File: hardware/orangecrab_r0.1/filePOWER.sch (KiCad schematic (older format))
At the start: 45 parts, among them J5 Conn_01x02_Male, U1 FAN53541, U10 NCP167, U2 FAN53541, U5 BQ24230, U7 FAN53541, U8 TPS51206

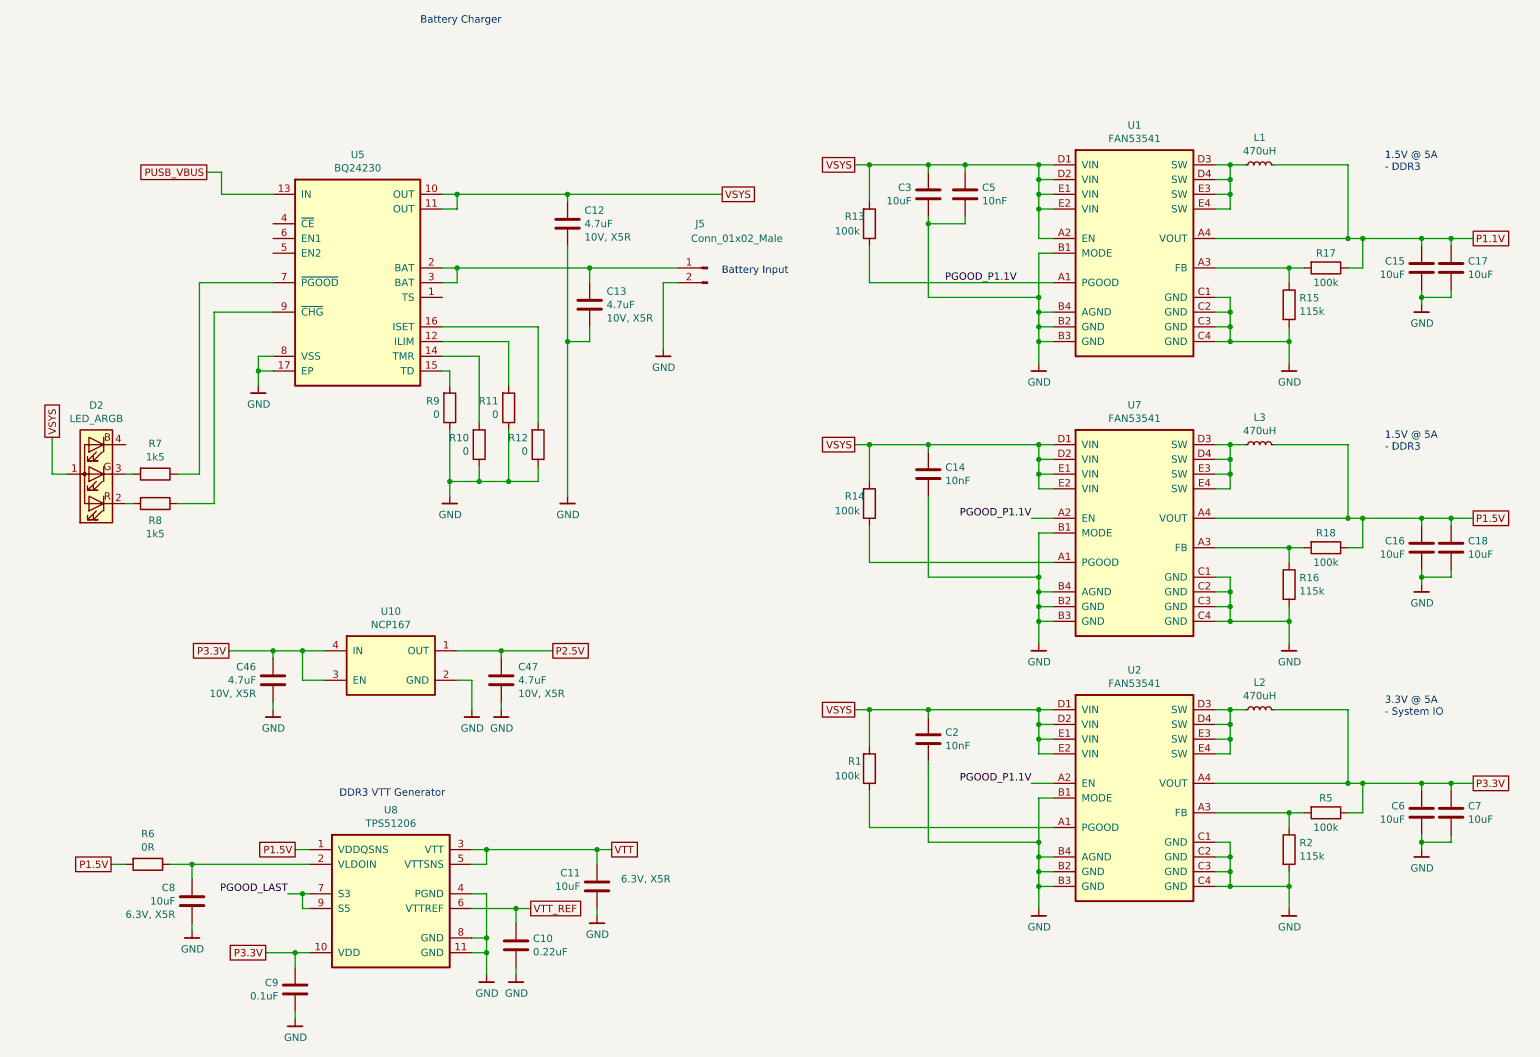
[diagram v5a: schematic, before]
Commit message: Completed 99% of routing.
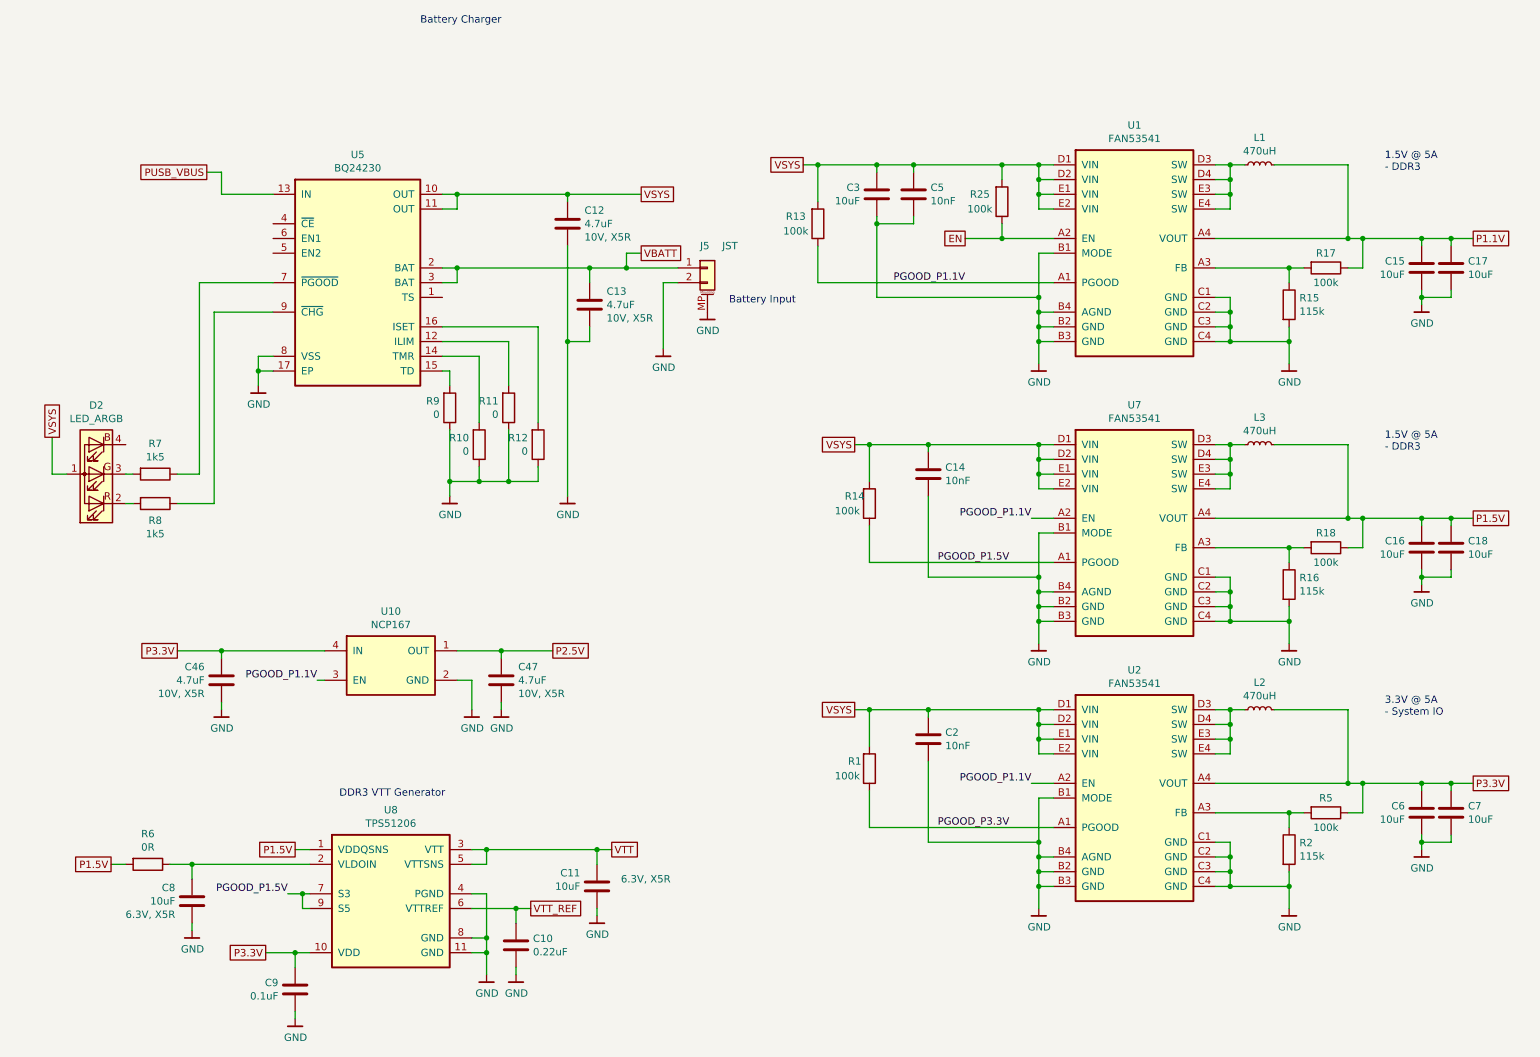
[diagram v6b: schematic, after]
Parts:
- removed J5: Conn_01x02_Male, gkl_conn:JST_PH_B2B-PH-SM4-TB_1x02-1MP_P2.00mm_Vertical, symbol Connector:Conn_01x02_Male
- added J5: JST, gkl_conn:JST_PH_B2B-PH-SM4-TB_1x02-1MP_P2.00mm_Vertical, symbol Connector_Generic_MountingPin:Conn_01x02_MountingPin
- added R25: 100k, Resistor_SMD:R_0201_0603Metric, symbol Device:R
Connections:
- net PGOOD_LAST is gone; now on net PGOOD_P1.5V: U8.7 (S3), U8.9 (S5)
- net GND: now also J5.2 (Pin_2), J5.MP (MountPin)
- net P3.3V: no longer U10.3 (EN)
- net PGOOD_P1.1V: now also U10.3 (EN)
- net VSYS: now also R25.2; no longer U1.A2 (EN)
- net PGOOD_P3.3V: now reaches R1.1, U2.A1 (PGOOD)
- net VBATT: now reaches C13.1, U5.2 (BAT), U5.3 (BAT)
- net VBATT: now also J5.1 (Pin_1)
- net PGOOD_P1.5V: now reaches R14.1, U7.A1 (PGOOD)
- new net EN: R25.1, U1.A2 (EN)
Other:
- moved on the sheet: C3, C46, C5, R13
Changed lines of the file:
@@
 Comment4 ""
 $EndDescr
-Text Notes 6050 1950 2    50   ~ 0
+Text Notes 6100 2150 2    50   ~ 0
 Battery Input
 Text Notes 3550 250  0    50   ~ 0
@@
 $EndComp
 $Comp
-L Connector:Conn_01x02_Male J5
-U 1 1 5D179AC3
-P 5500 1900
-F 0 "J5" H 5550 2200 50  0000 C CNN
-F 1 "Conn_01x02_Male" H 5300 2100 50  0000 C CNN
-F 2 "gkl_conn:JST_PH_B2B-PH-SM4-TB_1x02-1MP_P2.00mm_Vertical" H 5500 1900 50  0001 C CNN
-F 3 "~" H 5500 1900 50  0001 C CNN
-	1    5500 1900
-	-1   0    0    -1
-$EndComp
-$Comp
 L gkl_pmic:FAN53541 U2
 U 1 1 5D171FDD
@@
 $EndComp
 Wire Wire Line
-	7000 5250 7000 5300
-Wire Wire Line
 	7000 5800 7750 5800
 Connection ~ 7750 5800
@@
 Connection ~ 4700 1900
 Wire Wire Line
-	4700 1900 5300 1900
+	4700 1900 4950 1900
 Wire Wire Line
 	4550 1750 4550 2400
@@
 Text GLabel 6500 4900 0    50   UnSpc ~ 0
 VSYS
-Text GLabel 5600 1400 2    50   UnSpc ~ 0
+Text GLabel 5050 1400 2    50   UnSpc ~ 0
 VSYS
 Wire Wire Line
-	5600 1400 4550 1400
+	5050 1400 4550 1400
 Connection ~ 4550 1400
 Wire Wire Line
@@
 	7750 1500 7750 1400
 Wire Wire Line
-	7750 1200 7250 1200
+	7750 1200 7500 1200
 Wire Wire Line
 	7850 1200 7750 1200
@@
 	7750 1400 7750 1300
 Wire Wire Line
-	7850 1700 7750 1700
-Wire Wire Line
 	7850 2400 7750 2400
 Wire Wire Line
@@
 Connection ~ 7750 2200
 Wire Wire Line
-	7850 2000 6600 2000
-Wire Wire Line
-	6600 2000 6600 1750
+	7850 2000 6250 2000
+Wire Wire Line
+	6250 2000 6250 1750
 $Comp
 L Device:R R13
 U 1 1 5D42715D
-P 6600 1600
-F 0 "R13" H 6500 1550 50  0000 C CNN
-F 1 "100k" H 6450 1650 50  0000 C CNN
-F 2 "Resistor_SMD:R_0201_0603Metric" V 6530 1600 50  0001 C CNN
-F 3 "~" H 6600 1600 50  0001 C CNN
-	1    6600 1600
+P 6250 1600
+F 0 "R13" H 6100 1550 50  0000 C CNN
+F 1 "100k" H 6100 1650 50  0000 C CNN
+F 2 "Resistor_SMD:R_0201_0603Metric" V 6180 1600 50  0001 C CNN
+F 3 "~" H 6250 1600 50  0001 C CNN
+	1    6250 1600
 	1    0    0    1
 $EndComp
 Wire Wire Line
-	6600 1450 6600 1200
-Connection ~ 6600 1200
-Wire Wire Line
-	6600 1200 6500 1200
+	6250 1450 6250 1200
+Connection ~ 6250 1200
+Wire Wire Line
+	6250 1200 6150 1200
 $Comp
 L gkl_power:GND #PWR0113
@@
 	1    0    0    -1
 $EndComp
-Text Label 7600 2000 2    50   ~ 0
+Text Label 7250 2000 2    50   ~ 0
 PGOOD_P1.1V
 $Comp
 L Device:C C3
 U 1 1 5D42717F
-P 7000 1400
-F 0 "C3" H 6886 1354 50  0000 R CNN
-F 1 "10uF" H 6886 1445 50  0000 R CNN
-F 2 "Capacitor_SMD:C_0603_1608Metric" H 7038 1250 50  0001 C CNN
-F 3 "~" H 7000 1400 50  0001 C CNN
-	1    7000 1400
+P 6650 1400
+F 0 "C3" H 6536 1354 50  0000 R CNN
+F 1 "10uF" H 6536 1445 50  0000 R CNN
+F 2 "Capacitor_SMD:C_0603_1608Metric" H 6688 1250 50  0001 C CNN
+F 3 "~" H 6650 1400 50  0001 C CNN
+	1    6650 1400
 	1    0    0    1
 $EndComp
@@
 L Device:C C5
 U 1 1 5D427189
-P 7250 1400
-F 0 "C5" H 7135 1354 50  0000 R CNN
-F 1 "10nF" H 7135 1445 50  0000 R CNN
-F 2 "Capacitor_SMD:C_0201_0603Metric" H 7288 1250 50  0001 C CNN
-F 3 "~" H 7250 1400 50  0001 C CNN
-	1    7250 1400
+P 6900 1400
+F 0 "C5" H 6785 1354 50  0000 R CNN
+F 1 "10nF" H 6785 1445 50  0000 R CNN
+F 2 "Capacitor_SMD:C_0201_0603Metric" H 6938 1250 50  0001 C CNN
+F 3 "~" H 6900 1400 50  0001 C CNN
+	1    6900 1400
 	-1   0    0    1
 $EndComp
 Wire Wire Line
-	7250 1550 7250 1600
-Wire Wire Line
-	7250 1600 7000 1600
-Wire Wire Line
-	7000 1600 7000 2100
-Wire Wire Line
-	7000 2100 7750 2100
+	6900 1550 6900 1600
+Wire Wire Line
+	6900 1600 6650 1600
+Wire Wire Line
+	6650 1600 6650 2100
+Wire Wire Line
+	6650 2100 7750 2100
 Connection ~ 7750 2100
 Wire Wire Line
 	7750 2100 7750 2200
 Wire Wire Line
-	7000 1550 7000 1600
-Connection ~ 7000 1600
-Wire Wire Line
-	7000 1250 7000 1200
-Connection ~ 7000 1200
-Wire Wire Line
-	7000 1200 6600 1200
-Wire Wire Line
-	7250 1250 7250 1200
-Connection ~ 7250 1200
-Wire Wire Line
-	7250 1200 7000 1200
+	6650 1550 6650 1600
+Connection ~ 6650 1600
+Wire Wire Line
+	6650 1250 6650 1200
+Connection ~ 6650 1200
+Wire Wire Line
+	6650 1200 6250 1200
+Wire Wire Line
+	6900 1250 6900 1200
+Connection ~ 6900 1200
+Wire Wire Line
+	6900 1200 6650 1200
 Text GLabel 10700 1700 2    50   UnSpc ~ 0
 P1.1V
-Text GLabel 6500 1200 0    50   UnSpc ~ 0
+Text GLabel 6150 1200 0    50   UnSpc ~ 0
 VSYS
 Wire Wire Line
-	7750 1500 7750 1700
-Connection ~ 7750 1500
-Wire Wire Line
 	6600 3100 7000 3100
 Wire Wire Line
 	6600 4900 7000 4900
-Wire Wire Line
-	7000 5300 7000 5800
 $Comp
 L Device:LED_ARGB D2
@@
 Wire Wire Line
 	2800 6250 2750 6250
-Text Label 2650 6150 2    50   ~ 0
-PGOOD_LAST
 Wire Wire Line
 	2800 6150 2750 6150
@@
 L gkl_power:GND #PWR0145
 U 1 1 5D85A10F
-P 2550 4900
-F 0 "#PWR0145" H 2550 4650 50  0001 C CNN
-F 1 "GND" H 2553 4774 50  0000 C CNN
-F 2 "" H 2450 4550 50  0001 C CNN
-F 3 "" H 2550 4900 50  0001 C CNN
-	1    2550 4900
-	1    0    0    -1
-$EndComp
-Wire Wire Line
-	2750 4500 2550 4500
-Connection ~ 2750 4500
-Wire Wire Line
-	2750 4700 2750 4500
-Wire Wire Line
-	2900 4700 2750 4700
+P 2200 4900
+F 0 "#PWR0145" H 2200 4650 50  0001 C CNN
+F 1 "GND" H 2203 4774 50  0000 C CNN
+F 2 "" H 2100 4550 50  0001 C CNN
+F 3 "" H 2200 4900 50  0001 C CNN
+	1    2200 4900
+	1    0    0    -1
+$EndComp
+Wire Wire Line
+	2900 4700 2850 4700
 Wire Wire Line
 	3900 4700 3900 4900
@@
 	4100 4850 4100 4900
 Wire Wire Line
-	2550 4850 2550 4900
-Wire Wire Line
-	2550 4500 2250 4500
-Connection ~ 2550 4500
-Wire Wire Line
-	2550 4550 2550 4500
-Wire Wire Line
-	2900 4500 2750 4500
+	2200 4850 2200 4900
+Wire Wire Line
+	2200 4500 1900 4500
+Connection ~ 2200 4500
+Wire Wire Line
+	2200 4550 2200 4500
 Wire Wire Line
 	4100 4500 4450 4500
@@
 L Device:C C46
 U 1 1 5D757AA5
-P 2550 4700
-F 0 "C46" H 2665 4791 50  0000 L CNN
-F 1 "4.7uF" H 2665 4700 50  0000 L CNN
-F 2 "Capacitor_SMD:C_0402_1005Metric" H 2588 4550 50  0001 C CNN
-F 3 "~" H 2550 4700 50  0001 C CNN
-F 4 "10V, X5R" H 2665 4609 50  0000 L CNN "Info"
-	1    2550 4700
+P 2200 4700
+F 0 "C46" H 2315 4791 50  0000 L CNN
+F 1 "4.7uF" H 2315 4700 50  0000 L CNN
+F 2 "Capacitor_SMD:C_0402_1005Metric" H 2238 4550 50  0001 C CNN
+F 3 "~" H 2200 4700 50  0001 C CNN
+F 4 "10V, X5R" H 2315 4609 50  0000 L CNN "Info"
+	1    2200 4700
 	-1   0    0    -1
 $EndComp
-Text GLabel 2250 4500 0    50   UnSpc ~ 0
+Text GLabel 1900 4500 0    50   UnSpc ~ 0
 P3.3V
 $Comp
@@
 Wire Wire Line
 	7000 3450 7000 4000
+$Comp
+L Connector_Generic_MountingPin:Conn_01x02_MountingPin J5
+U 1 1 5D8317B6
+P 5500 1900
+F 0 "J5" H 5450 2050 50  0000 L CNN
+F 1 "JST" H 5600 2050 50  0000 L CNN
+F 2 "gkl_conn:JST_PH_B2B-PH-SM4-TB_1x02-1MP_P2.00mm_Vertical" H 5500 1900 50  0001 C CNN
+F 3 "~" H 5500 1900 50  0001 C CNN
+	1    5500 1900
+	1    0    0    -1
+$EndComp
+$Comp
+L gkl_power:GND #PWR0166
+U 1 1 5D8325AB
+P 5500 2200
+F 0 "#PWR0166" H 5500 1950 50  0001 C CNN
+F 1 "GND" H 5503 2074 50  0000 C CNN
+F 2 "" H 5400 1850 50  0001 C CNN
+F 3 "" H 5500 2200 50  0001 C CNN
+	1    5500 2200
+	1    0    0    -1
+$EndComp
+Text GLabel 5050 1800 2    50   UnSpc ~ 0
+VBATT
+Wire Wire Line
+	5050 1800 4950 1800
+Wire Wire Line
+	4950 1800 4950 1900
+Wire Wire Line
+	7000 5250 7000 5800
+Connection ~ 4950 1900
+Wire Wire Line
+	4950 1900 5300 1900
+Text Label 2850 4700 2    50   ~ 0
+PGOOD_P1.1V
+Wire Wire Line
+	2200 4500 2900 4500
+Text Label 7550 3900 2    50   ~ 0
+PGOOD_P1.5V
+Text Label 7550 5700 2    50   ~ 0
+PGOOD_P3.3V
+Text Label 2650 6150 2    50   ~ 0
+PGOOD_P1.5V
+Text GLabel 7250 1700 0    50   UnSpc ~ 0
+EN
+Wire Wire Line
+	7250 1700 7500 1700
+$Comp
+L Device:R R25
+U 1 1 5D9B61C6
+P 7500 1450
+F 0 "R25" H 7350 1400 50  0000 C CNN
+F 1 "100k" H 7350 1500 50  0000 C CNN
+F 2 "Resistor_SMD:R_0201_0603Metric" V 7430 1450 50  0001 C CNN
+F 3 "~" H 7500 1450 50  0001 C CNN
+	1    7500 1450
+	1    0    0    1
+$EndComp
+Wire Wire Line
+	7500 1600 7500 1700
+Connection ~ 7500 1700
+Wire Wire Line
+	7500 1700 7850 1700
+Wire Wire Line
+	7500 1300 7500 1200
+Connection ~ 7500 1200
+Wire Wire Line
+	7500 1200 6900 1200
 $EndSCHEMATC

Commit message: Completed DDR Routing Added logo to back of PCB Added Fiducials Neatened up power planes Generated Gerbers for PCB fab quote
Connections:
- net GND: now also U5.4 (~CE), U5.6 (EN1)
- net VSYS: now also U5.5 (EN2)
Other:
- note added: "Charge Current Set by ILIM"
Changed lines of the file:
@@
 Wire Wire Line
 	2200 1250 2200 1400
-Wire Wire Line
-	2200 1400 2550 1400
 Text GLabel 2100 1250 0    50   UnSpc ~ 0
 PUSB_VBUS
@@
 Wire Wire Line
 	7500 1200 6900 1200
+Wire Wire Line
+	2550 1700 2500 1700
+$Comp
+L gkl_power:GND #PWR?
+U 1 1 5E42D569
+P 2250 1700
+F 0 "#PWR?" H 2250 1450 50  0001 C CNN
+F 1 "GND" H 2253 1574 50  0000 C CNN
+F 2 "" H 2150 1350 50  0001 C CNN
+F 3 "" H 2250 1700 50  0001 C CNN
+	1    2250 1700
+	0    1    1    0
+$EndComp
+Wire Wire Line
+	2550 1600 2500 1600
+Wire Wire Line
+	2500 1600 2500 1700
+Connection ~ 2500 1700
+Wire Wire Line
+	2500 1700 2250 1700
+Wire Wire Line
+	2200 1400 2550 1400
+Text GLabel 1950 1800 0    50   UnSpc ~ 0
+VSYS
+Wire Wire Line
+	1950 1800 2550 1800
+Text Notes 950  1700 0    50   ~ 0
+Charge Current Set by ILIM
 $EndSCHEMATC
